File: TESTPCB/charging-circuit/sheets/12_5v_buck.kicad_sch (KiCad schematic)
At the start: 14 parts, among them P9 1.27mm/1*3p, U20 TPS54302DDCR_C311983

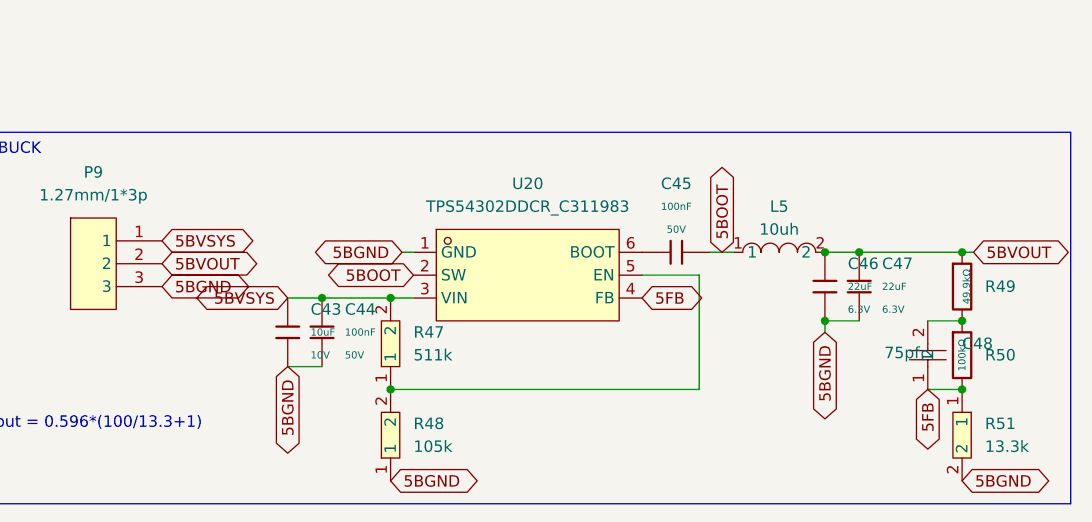
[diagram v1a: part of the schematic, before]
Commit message: Fixed formatting issues, now the hierachal sheets are all labeled as net labels and when we want to expose their pins we will make them into hierchal or global pins
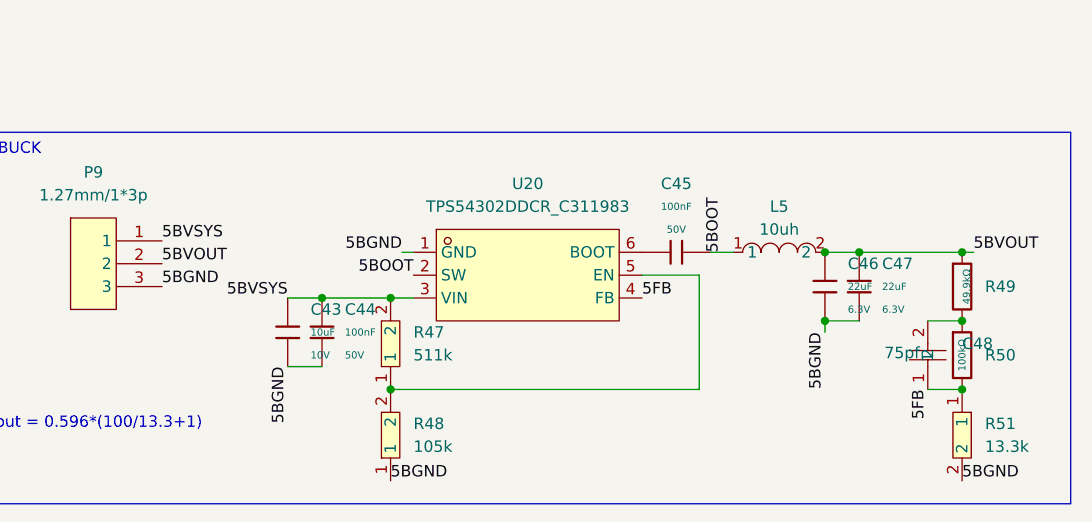
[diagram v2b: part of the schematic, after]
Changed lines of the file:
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@@
 		)
 	)
-	(global_label "5BGND"
-		(shape bidirectional)
+	(label "5BGND"
 		(at 187.96 104.14 0)
 		(effects
@@
 			(justify left bottom)
 		)
-		(property "Intersheetrefs" "${INTERSHEET_REFS}"
-			(at 187.96 104.14 0)
-			(effects
-				(font
-					(size 1.27 1.27)
-				)
-				(hide yes)
-			)
-		)
 	)
-	(global_label "5BVSYS"
-		(shape bidirectional)
+	(label "5BVSYS"
 		(at 99.06 77.47 0)
 		(effects
@@
 			(justify left bottom)
 		)
-		(property "Intersheetrefs" "${INTERSHEET_REFS}"
-			(at 99.06 77.47 0)
-			(effects
-				(font
-					(size 1.27 1.27)
-				)
-				(hide yes)
-			)
-		)
 	)
-	(global_label "5BOOT"
-		(shape bidirectional)
+	(label "5BOOT"
 		(at 161.29 78.74 90)
 		(effects
@@
 			(justify left bottom)
 		)
-		(property "Intersheetrefs" "${INTERSHEET_REFS}"
-			(at 161.29 78.74 0)
-			(effects
-				(font
-					(size 1.27 1.27)
-				)
-				(hide yes)
-			)
-		)
 	)
-	(global_label "5BOOT"
-		(shape bidirectional)
+	(label "5BOOT"
 		(at 127 81.28 180)
 		(effects
@@
 			(justify right bottom)
 		)
-		(property "Intersheetrefs" "${INTERSHEET_REFS}"
-			(at 127 81.28 0)
-			(effects
-				(font
-					(size 1.27 1.27)
-				)
-				(hide yes)
-			)
-		)
 	)
-	(global_label "5BVOUT"
-		(shape bidirectional)
+	(label "5BVOUT"
 		(at 189.23 78.74 0)
 		(effects
@@
 			(justify left bottom)
 		)
-		(property "Intersheetrefs" "${INTERSHEET_REFS}"
-			(at 189.23 78.74 0)
-			(effects
-				(font
-					(size 1.27 1.27)
-				)
-				(hide yes)
-			)
-		)
 	)
-	(global_label "5BVSYS"
-		(shape bidirectional)
+	(label "5BVSYS"
 		(at 113.03 83.82 180)
 		(effects
@@
 			(justify right bottom)
 		)
-		(property "Intersheetrefs" "${INTERSHEET_REFS}"
-			(at 113.03 83.82 0)
-			(effects
-				(font
-					(size 1.27 1.27)
-				)
-				(hide yes)
-			)
-		)
 	)
-	(global_label "5BGND"
-		(shape bidirectional)
+	(label "5BGND"
 		(at 99.06 82.55 0)
 		(effects
@@
 			(justify left bottom)
 		)
-		(property "Intersheetrefs" "${INTERSHEET_REFS}"
-			(at 99.06 82.55 0)
-			(effects
-				(font
-					(size 1.27 1.27)
-				)
-				(hide yes)
-			)
-		)
 	)
-	(global_label "5BVOUT"
-		(shape bidirectional)
+	(label "5BVOUT"
 		(at 99.06 80.01 0)
 		(effects
@@
 			(justify left bottom)
 		)
-		(property "Intersheetrefs" "${INTERSHEET_REFS}"
-			(at 99.06 80.01 0)
-			(effects
-				(font
-					(size 1.27 1.27)
-				)
-				(hide yes)
-			)
-		)
 	)
-	(global_label "5BGND"
-		(shape bidirectional)
+	(label "5BGND"
 		(at 172.72 87.63 270)
 		(effects
@@
 			(justify right bottom)
 		)
-		(property "Intersheetrefs" "${INTERSHEET_REFS}"
-			(at 172.72 87.63 0)
-			(effects
-				(font
-					(size 1.27 1.27)
-				)
-				(hide yes)
-			)
-		)
 	)
-	(global_label "5BGND"
-		(shape bidirectional)
+	(label "5BGND"
 		(at 125.73 78.74 180)
 		(effects
@@
 			(justify right bottom)
 		)
-		(property "Intersheetrefs" "${INTERSHEET_REFS}"
-			(at 125.73 78.74 0)
-			(effects
-				(font
-					(size 1.27 1.27)
-				)
-				(hide yes)
-			)
-		)
 	)
-	(global_label "5FB"
-		(shape bidirectional)
+	(label "5FB"
 		(at 152.4 83.82 0)
 		(effects
@@
 			(justify left bottom)
 		)
-		(property "Intersheetrefs" "${INTERSHEET_REFS}"
-			(at 152.4 83.82 0)
-			(effects
-				(font
-					(size 1.27 1.27)
-				)
-				(hide yes)
-			)
-		)
 	)
-	(global_label "5BGND"
-		(shape bidirectional)
+	(label "5BGND"
 		(at 124.46 104.14 0)
 		(effects
@@
 			(justify left bottom)
 		)
-		(property "Intersheetrefs" "${INTERSHEET_REFS}"
-			(at 124.46 104.14 0)
-			(effects
-				(font
-					(size 1.27 1.27)
-				)
-				(hide yes)
-			)
-		)
 	)
-	(global_label "5BGND"
-		(shape bidirectional)
+	(label "5BGND"
 		(at 113.03 91.44 270)
 		(effects
@@
 			(justify right bottom)
 		)
-		(property "Intersheetrefs" "${INTERSHEET_REFS}"
-			(at 113.03 91.44 0)
-			(effects
-				(font
-					(size 1.27 1.27)
-				)
-				(hide yes)
-			)
-		)
 	)
-	(global_label "5FB"
-		(shape bidirectional)
+	(label "5FB"
 		(at 184.15 93.98 270)
 		(effects
@@
 			(justify right bottom)
 		)
-		(property "Intersheetrefs" "${INTERSHEET_REFS}"
-			(at 184.15 93.98 0)
-			(effects
-				(font
-					(size 1.27 1.27)
-				)
-				(hide yes)
-			)
-		)
 	)
